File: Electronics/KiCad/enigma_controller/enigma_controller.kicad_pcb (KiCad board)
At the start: 6 copper layers, 267.3 x 149.5 mm, 46 parts, among them IC1 SN74LVC257ADR, IC10 MCP23017-E_SO, IC2 SN74LVC257ADR, IC3 SN74LVC257ADR, IC4 SN74LVC257ADR, IC5 SN74LVC257ADR, IC6 SN74LVC257ADR, IC7 SN74LVC257ADR, IC9 MCP23017-E_SO, J1 Conn_02x07_Odd_Even, J10 0936263006, J11 Conn_02x05_Odd_Even, J12 Conn_01x02, J13 Conn_01x02, J14 USB_C_Receptacle_PowerOnly_6P, J15 Conn_01x02, J16 Conn_01x02, J17 Conn_01x02, J18 Conn_01x02, J19 Conn_01x02, J2 Conn_02x07_Odd_Even, J20 Conn_01x02, J21 Conn_02x05_Odd_Even, J22 Conn_02x05_Odd_Even, J23 Conn_01x02, J24 Conn_01x02, J3 USB1040-GF-L-B, J4 Conn_01x02, J5 46765-0301, J6 Conn_02x05_Odd_Even, J7 Conn_02x07_Odd_Even, J8 USB3_A_Stacked, J9 Conn_02x07_Odd_Even, M1 Fan_4pin

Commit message: Re-organised PCB Layout for better usage of space.
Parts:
- moved BT1 170.6 mm to (220.8, 58.1), turned to -90 degrees
- moved J4 127.9 mm to (267.5, 19.6)
- moved LED2 127.9 mm to (255.1, 19.3)
- moved R2 127.9 mm to (255.1, 22.3)
- moved J12 127.9 mm to (271.9, 19.6)
- moved J13 127.9 mm to (276.1, 19.6)
- moved LED1 127.9 mm to (251.0, 19.3)
- moved R1 127.9 mm to (251.0, 22.4)
- moved LED87 127.9 mm to (259.4, 19.3)
- moved R89 127.9 mm to (259.4, 22.3)
- moved S2 105.0 mm to (219.3, 22.2)
- moved S1 105.0 mm to (209.5, 22.1)
- moved R3 95.9 mm to (232.7, 157.0)
- moved H1 95.1 mm to (214.0, 88.7)
- moved J8 94.4 mm to (212.1, 152.6)
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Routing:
- net Net-(J10-A_YELLOW): track 8.55 -> 5.77 mm
- net Net-(J10-A_GREEN): track 5.99 -> 3.28 mm
- added copper zone on In3.Cu, net +3V3
- added copper zone on In2.Cu, net +5V
- added copper zone on In4.Cu, net /SHIELD
- added copper zone on In1.Cu, net GND
- removed copper zone on In4.Cu, net +3V3
- removed copper zone on In1.Cu, net +5V
- removed copper zone on In2.Cu, net /SHIELD
- removed copper zone on In3.Cu, net GND
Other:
- board text added: "Board Stackup L1 = Fast Signals + JTAG L2 = GND L3 = +5V L4 = +3V3 L5 = SHIELD L6 = Slow Signals"

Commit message: Controller updates based on CM5IO board schematics.
Added some extra datasheets.
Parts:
- removed J12, J13, J4: Conn_01x02, Connector_PinHeader_2.54mm:PinHeader_1x02_P2.54mm_Vertical
- removed R89: ERA2AEB201X, Enigma_Components:ERA2AED122X
- added C1: 100nF, PCM_JLCPCB:C_0402, F.Cu at (255.0, 118.4)
- added C10: 100nF, PCM_JLCPCB:C_0402, F.Cu at (72.2, 141.5)
- added C11: 100nF, PCM_JLCPCB:C_0402, F.Cu at (40.8, 99.5)
- added C12: 100nF, PCM_JLCPCB:C_0402, F.Cu at (69.5, 84.7)
- added C13: 100nF, PCM_JLCPCB:C_0402, F.Cu at (135.7, 72.7)
- added C14: 100nF, PCM_JLCPCB:C_0402, F.Cu at (41.4, 70.5)
- added C15: 100nF, PCM_JLCPCB:C_0402, F.Cu at (42.1, 48.5)
- added C16: 100nF, PCM_JLCPCB:C_0402, F.Cu at (75.4, 31.6)
- added C17: 100nF, PCM_JLCPCB:C_0402, F.Cu at (135.8, 91.3)
- added C18: 10uF, PCM_JLCPCB:C_0603, F.Cu at (165.9, 119.9)
- added C19: 10uF, PCM_JLCPCB:C_0603, F.Cu at (166.0, 134.5)
- added C2: 100nF, PCM_JLCPCB:C_0402, F.Cu at (255.0, 119.6)
- added C3: 10uF, PCM_JLCPCB:C_0603, F.Cu at (166.0, 136.5)
- added C4: 100uF_25V, Capacitor_THT:CP_Radial_D6.3mm_P2.50mm, F.Cu at (166.8, 130.0)
- added C7: 100nF, PCM_JLCPCB:C_0402, F.Cu at (192.2, 139.5)
- added C8: 100nF, PCM_JLCPCB:C_0402, F.Cu at (196.5, 139.5)
- added C9: 100nF, PCM_JLCPCB:C_0402, F.Cu at (40.0, 118.3)
- added H2: MountingHole_Pad, MountingHole:MountingHole_4.3mm_M4_Pad_Via, F.Cu at (43.3, 34.7)
- added H3: MountingHole_Pad, MountingHole:MountingHole_4.3mm_M4_Pad_Via, F.Cu at (43.3, 142.0)
- added H4: MountingHole_Pad, MountingHole:MountingHole_4.3mm_M4_Pad_Via, F.Cu at (257.8, 34.7)
- added H5: MountingHole_Pad, MountingHole:MountingHole_4.3mm_M4_Pad_Via, F.Cu at (134.5, 118.9)
- added H6: MountingHole_Pad, MountingHole:MountingHole_4.3mm_M4_Pad_Via, F.Cu at (257.8, 142.0)
- added H7: MountingHole_Pad, MountingHole:MountingHole_4.3mm_M4_Pad_Via, F.Cu at (169.5, 65.7)
- added IC11: RT9742SNGV, Enigma_Components:SOT95P279X130-3N, F.Cu at (194.3, 140.2)
- added IC8: AP22653W6-7, Enigma_Components:SOT95P280X145-6N, F.Cu at (165.8, 123.3)
- added J25: Conn_01x02, Connector_PinHeader_2.54mm:PinHeader_1x02_P2.54mm_Vertical, F.Cu at (258.4, 45.0)
- added J26: Conn_01x02, Connector_PinHeader_2.54mm:PinHeader_1x02_P2.54mm_Vertical, F.Cu at (258.4, 81.4)
- added J27: Conn_01x02, Connector_PinHeader_2.54mm:PinHeader_1x02_P2.54mm_Vertical, F.Cu at (96.9, 70.3)
- added J28: Conn_02x03_Odd_Even, Connector_PinHeader_2.54mm:PinHeader_2x03_P2.54mm_Vertical, F.Cu at (240.3, 36.9)
- added R10: 1kΩ, PCM_JLCPCB:R_0402, F.Cu at (258.5, 91.3)
- added R5: 2.2kΩ, PCM_JLCPCB:R_0402, F.Cu at (255.3, 112.3)
- added R6: 2.2kΩ, PCM_JLCPCB:R_0402, F.Cu at (218.2, 86.6)
- added R7: 2.2kΩ, PCM_JLCPCB:R_0402, F.Cu at (219.2, 93.4)
- added R8: 10kΩ, PCM_JLCPCB:R_0402, F.Cu at (190.3, 73.8)
- added R9: 15kΩ, PCM_JLCPCB:R_0402, F.Cu at (165.3, 126.0)
- R3, R4: value ERA2AEB201X -> 470Ω; footprint Enigma_Components:ERA2AED122X -> PCM_JLCPCB:R_0402
- moved J17 183.2 mm to (96.9, 120.3), turned to 0 degrees
- moved IC6 109.7 mm to (47.9, 49.8), turned to 90 degrees
- moved IC7 100.1 mm to (74.1, 37.4)
- moved IC5 96.8 mm to (47.2, 71.7), turned to 90 degrees
- moved J3 92.7 mm to (184.3, 113.1), turned to -90 degrees
- moved IC2 86.2 mm to (73.3, 135.6), turned to 180 degrees
- moved LED2 80.4 mm to (261.5, 99.4), turned to 180 degrees
- moved IC3 78.5 mm to (46.8, 100.7), turned to 90 degrees
- moved R2 77.2 mm to (258.5, 99.4), turned to 180 degrees
- moved LED1 76.7 mm to (261.5, 95.3), turned to 180 degrees
- moved R1 73.3 mm to (258.4, 95.3), turned to 180 degrees
- moved LED87 72.0 mm to (261.5, 91.3), turned to 180 degrees
- moved IC1 68.1 mm to (46.1, 119.5), turned to 90 degrees
- moved IC4 65.1 mm to (75.3, 86.0), turned to 90 degrees
- moved M1 60.1 mm to (183.2, 77.6)
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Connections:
- H1 pad 111: +3V3 -> /VBUS_EN
- H1 pad 20: Net-(H1A-EEPROM_nWP) -> /EEPROM_nWP
- H1 pad 35: unconnected-(H1A-ID_SC-Pad35) -> Net-(H1A-ID_SC)
- H1 pad 36: unconnected-(H1A-ID_SD-Pad36) -> Net-(H1A-ID_SD)
- H1 pad 89: Net-(H1A-WL_nDisable) -> /WL_nDisable
- H1 pad 91: Net-(H1A-BT_nDisable) -> /BT_nDisable
- J3 pad 1: +5V -> /VBUS
- J5 pad 19: +5V -> /HDMI_5V
- J8 pad 1: +5V -> /VBUS
- J8 pad 10: +5V -> /VBUS
- S1 pad 1: unconnected-(S1-COM-Pad1) -> GND
- S2 pad 1: unconnected-(S2-COM-Pad1) -> GND
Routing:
- net Net-(J10-A_YELLOW): track 5.77 -> 0.00 mm
- net Net-(J10-A_GREEN): track 3.28 -> 0.00 mm
- net +3V3: track 2.71 -> 0.00 mm, vias 2 -> 0
- net Net-(LED1-Pad2): track 1.78 -> 0.00 mm
- net Net-(LED87-Pad2): track 1.74 -> 0.00 mm
- net Net-(LED2-Pad2): track 1.74 -> 0.00 mm
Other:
- board size 267.3 x 149.5 mm -> 227.9 x 120.8 mm

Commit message: PCB Layout [AS-Review-1]
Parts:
- moved H1 41.8 mm to (190.3, 93.7), turned to -90 degrees
- moved C17 34.7 mm to (169.9, 84.6)
- moved IC10 34.7 mm to (162.8, 67.9)
- moved IC9 34.7 mm to (162.8, 86.5)
- moved C13 34.7 mm to (169.8, 66.0)
- moved J3 29.7 mm to (165.3, 135.9), turned to 90 degrees
- moved M1 25.4 mm to (203.7, 62.8), turned to 180 degrees
- moved BT1 24.9 mm to (230.3, 55.2), turned to 0 degrees
- moved H7 24.6 mm to (189.1, 50.8)
- moved C3 23.4 mm to (160.6, 113.7), turned to 90 degrees
- moved C19 21.1 mm to (162.5, 113.7), turned to 90 degrees
- moved H4 15.6 mm to (242.6, 30.9)
- moved LED2 15.6 mm to (246.3, 95.7)
- moved S1 15.6 mm to (205.9, 30.4)
- moved H6 15.6 mm to (242.6, 138.3)
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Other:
- board size 227.9 x 120.8 mm -> 199.9 x 120.8 mm

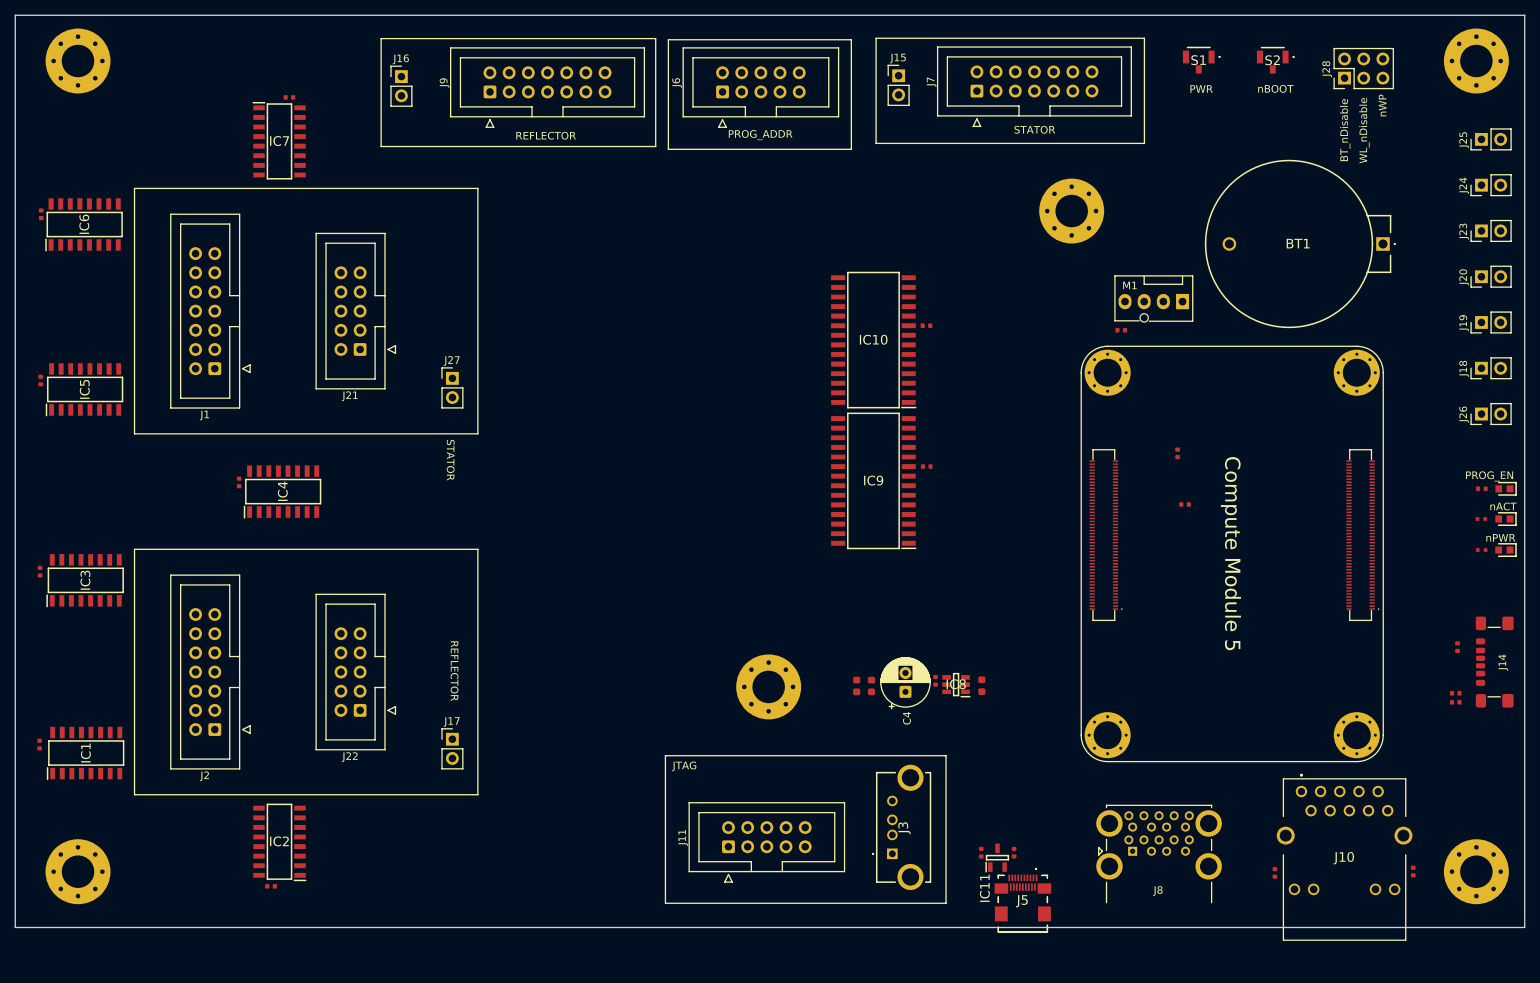
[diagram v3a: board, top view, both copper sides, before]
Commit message: Added ESD Protection.
Also updated some components to follow reference CM5IO board.
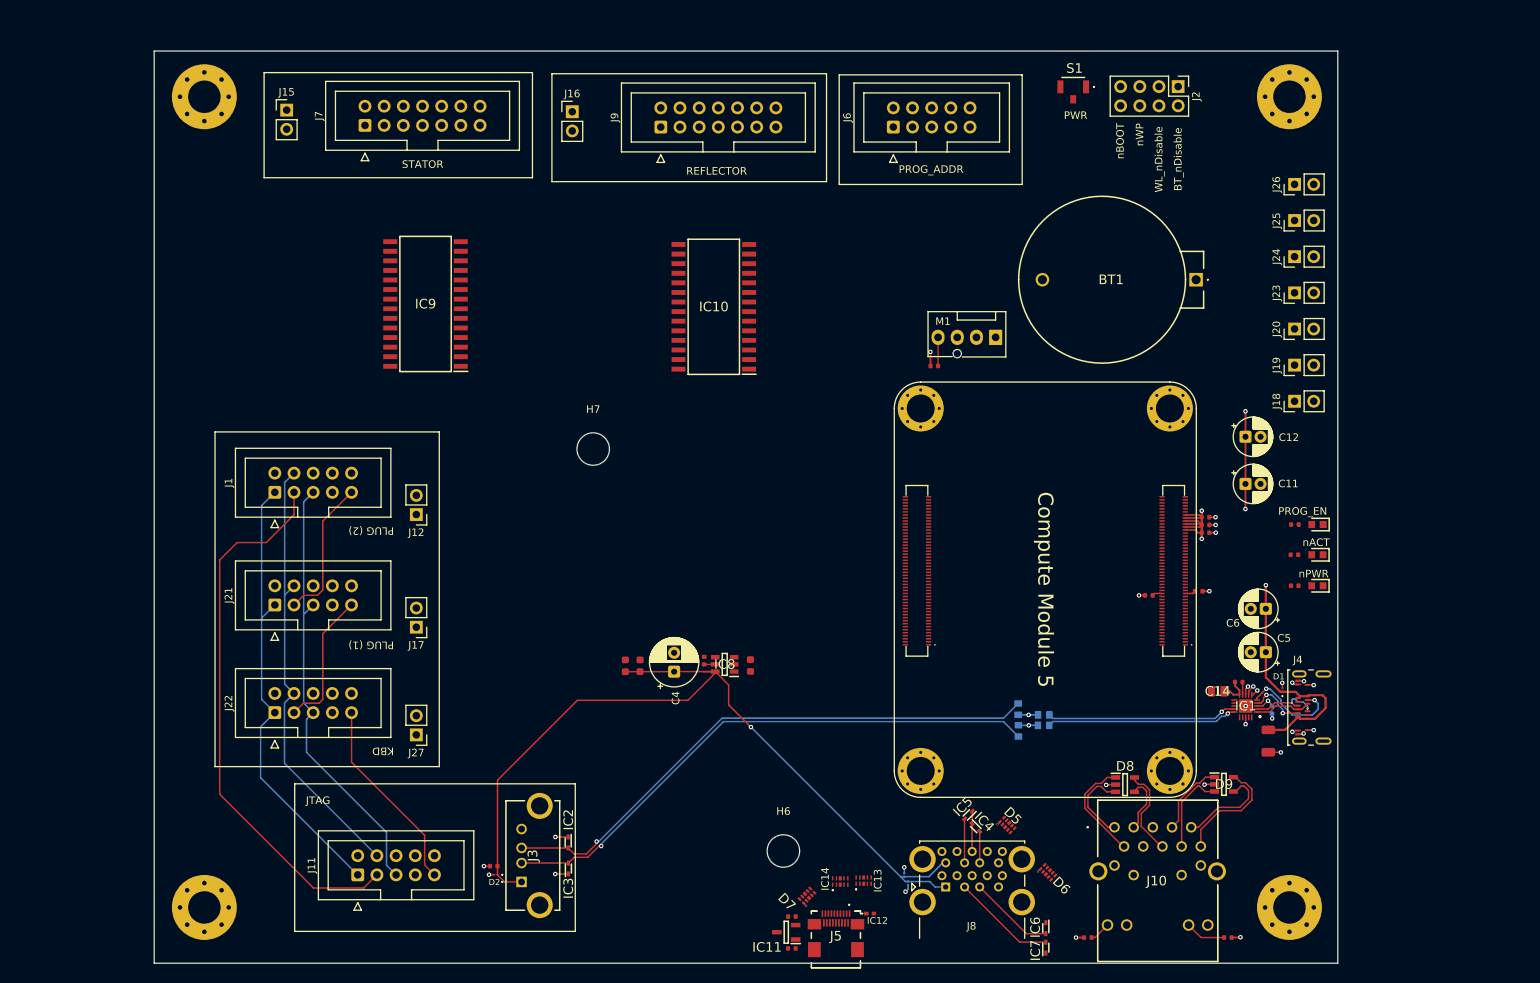
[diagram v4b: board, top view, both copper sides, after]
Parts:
- removed C10, C17: 100nF, PCM_JLCPCB:C_0402
- removed J14: USB_C_Receptacle_PowerOnly_6P, Connector_USB:USB_C_Receptacle_GCT_USB4135-GF-A_6P_TopMnt_Horizontal
- removed J28: Conn_02x03_Odd_Even, Connector_PinHeader_2.54mm:PinHeader_2x03_P2.54mm_Vertical
- removed S2: B3U-1100PM, Enigma_Components:B3U1100PM
- added C5: 4.7uF 50V, Capacitor_THT:CP_Radial_D5.0mm_P2.00mm, F.Cu at (214.8, 109.2)
- added C6: 4.7uF 50V, Capacitor_THT:CP_Radial_D5.0mm_P2.00mm, F.Cu at (214.8, 103.5)
- added D1: ESD441DPLR, Enigma_Components:ESD441DPLR, F.Cu at (217.0, 114.2)
- added D2: ESD441DPLR, Enigma_Components:ESD441DPLR, F.Cu at (112.8, 138.7)
- added D3: ESD441DPLR, Enigma_Components:ESD441DPLR, B.Cu at (166.9, 138.7)
- added D4: ESD441DPLR, Enigma_Components:ESD441DPLR, B.Cu at (167.4, 139.8)
- added D5: TPD4E02B04DQAR, Enigma_Components:DQA(R-PUSON-N10), F.Cu at (180.5, 132.1)
- added D6: TPD4E02B04DQAR, Enigma_Components:DQA(R-PUSON-N10), F.Cu at (185.9, 138.4)
- added D7: TPD4E05U06DQAR, Enigma_Components:DQA(R-PUSON-N10), F.Cu at (154.0, 141.5)
- added D8: ESDS314DBVR, Enigma_Components:SOT95P280X145-5N, F.Cu at (196.1, 126.8)
- added D9: ESDS314DBVR, Enigma_Components:SOT95P280X145-5N, F.Cu at (209.2, 126.7)
- added IC12: TPD1E05U06DPYT, Enigma_Components:TPD1E05U06DPYT, F.Cu at (162.4, 143.8)
- added IC13: ESD224DQAR, Enigma_Components:ESD224DQAR, F.Cu at (161.5, 139.5)
- added IC14: ESD224DQAR, Enigma_Components:ESD224DQAR, F.Cu at (158.4, 139.6)
- added J12: Conn_01x02, Connector_PinHeader_2.54mm:PinHeader_1x02_P2.54mm_Vertical, F.Cu at (102.3, 91.0)
- added J4: USB_C_Receptacle_USB2.0_16P, Connector_USB:USB_C_Receptacle_Amphenol_124019772112A, F.Cu at (222.2, 116.6)
- added R11: RCA06030000ZSEA, Enigma_Components:RESC1608X50N, B.Cu at (182.0, 116.8)
- added R12: RCA06030000ZSEA, Enigma_Components:RESC1608X50N, B.Cu at (185.3, 117.5)
- added R13: RCA06030000ZSEA, Enigma_Components:RESC1608X50N, B.Cu at (182.0, 119.6)
- added R14: RCA06030000ZSEA, Enigma_Components:RESC1608X50N, B.Cu at (185.3, 118.9)
- C11, C12: value 100nF -> 4.7uF 50V; footprint PCM_JLCPCB:C_0402 -> Capacitor_THT:CP_Radial_D5.0mm_P2.00mm
- C13: value 100nF -> 2.2uF; footprint PCM_JLCPCB:C_0402 -> PCM_JLCPCB:C_1206
- C14: value 100nF -> CL21B105KAFNNNG; footprint PCM_JLCPCB:C_0402 -> Enigma_Components:CAPC2012X135N
- C15: moved to B.Cu
- H6, H7: value MountingHole_Pad -> MountingHole; footprint MountingHole:MountingHole_4.3mm_M4_Pad_Via -> MountingHole:MountingHole_4.3mm_M4
- IC1: value SN74LVC257ADR -> TPD8S300ARUKR; footprint Enigma_Components:SOIC127P600X175-16N -> Enigma_Components:QFN40P300X300X80-21N-D
- IC2, IC3, IC4, IC5, IC6, IC7: value SN74LVC257ADR -> ESD321DYAR; footprint Enigma_Components:SOIC127P600X175-16N -> Enigma_Components:SODFL1608X77N
- J1: value Conn_02x07_Odd_Even -> Conn_02x05_Odd_Even; footprint Connector_IDC:IDC-Header_2x07_P2.54mm_Vertical -> Connector_IDC:IDC-Header_2x05_P2.54mm_Vertical
- J10: value 0936263006 -> A70-112-331N126; footprint Enigma_Components:0936263006 -> Enigma_Components:A70112331N126
- J2: value Conn_02x07_Odd_Even -> Conn_02x04_Odd_Even; footprint Connector_IDC:IDC-Header_2x07_P2.54mm_Vertical -> Connector_PinHeader_2.54mm:PinHeader_2x04_P2.54mm_Vertical
- R1, R2: value ERA2AEB201X -> 470Ω; footprint Enigma_Components:ERA2AED122X -> PCM_JLCPCB:R_0402
- R5: value 2.2kΩ -> 100kΩ
- moved C15 175.7 mm to (215.6, 116.9), turned to 90 degrees
- moved C14 161.2 mm to (208.4, 114.4), turned to 0 degrees
- moved C11 160.1 mm to (212.1, 86.9), turned to 0 degrees
- moved IC6 157.7 mm to (185.6, 145.8), turned to -90 degrees
- moved C9 157.3 mm to (206.8, 91.4), turned to 0 degrees
- moved IC1 153.7 mm to (212.1, 116.4), turned to 180 degrees
- moved J2 153.4 mm to (203.2, 34.3), turned to -90 degrees
- moved IC7 147.3 mm to (185.6, 148.4), turned to 90 degrees
- moved C12 133.4 mm to (212.1, 80.7), turned to 0 degrees
- moved IC5 129.8 mm to (175.4, 130.8), turned to -135 degrees
- moved C16 105.3 mm to (112.5, 137.6), turned to 0 degrees
- moved IC4 101.9 mm to (176.4, 132.4), turned to -45 degrees
- moved H6 91.8 mm to (150.9, 135.6)
- moved J15 81.2 mm to (85.1, 37.4)
- moved J7 81.2 mm to (95.5, 39.5)
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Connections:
- net /HDMI0_CEC renamed /enigma_controller_HS/HDMI0_CEC
- net /HDMI0_HOT_PLUG renamed /enigma_controller_HS/HDMI0_HOT_PLUG
- net /HDMI0_SCL renamed /enigma_controller_HS/HDMI0_SCL
- net /HDMI0_SDA renamed /enigma_controller_HS/HDMI0_SDA
- net /HDMI_5V renamed /enigma_controller_HS/HDMI_5V
- net /USB3_0_RX_N renamed /enigma_controller_HS/USB3_0_RX_N
- net /USB3_0_RX_P renamed /enigma_controller_HS/USB3_0_RX_P
- net /USB3_0_TX_N renamed /enigma_controller_HS/USB3_0_TX_N
- net /USB3_0_TX_P renamed /enigma_controller_HS/USB3_0_TX_P
- net /USB3_1_RX_N renamed /enigma_controller_HS/USB3_1_RX_N
- net /USB3_1_RX_P renamed /enigma_controller_HS/USB3_1_RX_P
- net /USB3_1_TX_N renamed /enigma_controller_HS/USB3_1_TX_N
- net /USB3_1_TX_P renamed /enigma_controller_HS/USB3_1_TX_P
- net /VBUS_EN renamed /enigma_controller_HS/VBUS_EN
- C13 pad 1: +3V3 -> +5V
- C14 pad 1: +3V3 -> GND
- C14 pad 2: GND -> +3V3
- C15 pad 2: GND -> Net-(IC1-VBIAS)
- C16 pad 1: +3V3 -> GND
- C16 pad 2: GND -> /VBUS
- C9 pad 1: +3V3 -> +5V
- H1 pad 103: /JTAG_USB_N -> /USB_DN
- H1 pad 105: /JTAG_USB_P -> /USB_DP
- H1 pad 134: /USB3_0_DP -> /enigma_controller_HS/USB3_0_DP
- H1 pad 136: /USB3_0_DM -> /enigma_controller_HS/USB3_0_DM
- H1 pad 163: /USB3_1_DP -> /enigma_controller_HS/USB3_1_DP
- H1 pad 165: /USB3_1_DM -> /enigma_controller_HS/USB3_1_DM
- H1 pad 170: /HDMI0_TX2_P -> /enigma_controller_HS/HDMI0_TX2_P
- H1 pad 172: /HDMI0_TX2_N -> /enigma_controller_HS/HDMI0_TX2_N
- H1 pad 176: /HDMI0_TX1_P -> /enigma_controller_HS/HDMI0_TX1_P
- H1 pad 178: /HDMI0_TX1_N -> /enigma_controller_HS/HDMI0_TX1_N
- H1 pad 182: /HDMI0_TX0_P -> /enigma_controller_HS/HDMI0_TX0_P
- H1 pad 184: /HDMI0_TX0_N -> /enigma_controller_HS/HDMI0_TX0_N
- H1 pad 188: /HDMI0_CLK_P -> /enigma_controller_HS/HDMI0_CLK_P
- H1 pad 190: /HDMI0_CLK_N -> /enigma_controller_HS/HDMI0_CLK_N
- H1 pad 93: Net-(H1A-nRPIBOOT) -> /nRPIBOOT
- IC1 pad 1: /PROG_EN -> /C_D+
- IC1 pad 10: /enigma_controller_prog/pBIN_IN_A3 -> +3V3
- IC1 pad 11: /enigma_controller_prog/rBIN_IN_A3 -> /PD_CC2
- IC1 pad 12: /oBIN_IN_A4 -> /PD_CC1
- IC1 pad 13: /enigma_controller_prog/pBIN_IN_A4 -> GND
- IC1 pad 14: /enigma_controller_prog/rBIN_IN_A4 -> /FLASH_D+
- IC1 pad 15: GND -> /FLASH_D-
- IC1 pad 16: +3V3 -> unconnected-(IC1-D4-Pad16)
- IC1 pad 2: /enigma_controller_prog/rBIN_IN_A1 -> /C_D-
- IC1 pad 3: /enigma_controller_prog/pBIN_IN_A1 -> Net-(IC1-VBIAS)
- IC1 pad 4: /oBIN_IN_A1 -> /C_CC1
- IC1 pad 5: /enigma_controller_prog/rBIN_IN_A2 -> /C_CC2
- IC1 pad 6: /enigma_controller_prog/pBIN_IN_A2 -> GND
- IC1 pad 7: /oBIN_IN_A2 -> GND
- IC1 pad 9: /oBIN_IN_A3 -> Net-(IC1-~{FLT})
- IC10 pad 1: /enigma_controller_prog/pBIN_IN_B1 -> /pBIN_IN_B1
- IC10 pad 2: /enigma_controller_prog/pBIN_IN_B2 -> /pBIN_IN_B2
- IC10 pad 21: /enigma_controller_prog/pBIN_OUT_B1 -> /pBIN_OUT_B1
- IC10 pad 22: /enigma_controller_prog/pBIN_OUT_B2 -> /pBIN_OUT_B2
- IC10 pad 23: /enigma_controller_prog/pBIN_OUT_B3 -> /pBIN_OUT_B3
- IC10 pad 24: /enigma_controller_prog/pBIN_OUT_B4 -> /pBIN_OUT_B4
- IC10 pad 25: /enigma_controller_prog/pBIN_OUT_B5 -> /pBIN_OUT_B5
- IC10 pad 26: /enigma_controller_prog/pBIN_OUT_B6 -> /pBIN_OUT_B6
- IC10 pad 27: /enigma_controller_prog/pBIN_OUT_nOE_B -> /pBIN_OUT_nOE_B
- IC10 pad 3: /enigma_controller_prog/pBIN_IN_B3 -> /pBIN_IN_B3
- IC10 pad 4: /enigma_controller_prog/pBIN_IN_B4 -> /pBIN_IN_B4
- IC10 pad 5: /enigma_controller_prog/pBIN_IN_B5 -> /pBIN_IN_B5
- IC10 pad 6: /enigma_controller_prog/pBIN_IN_B6 -> /pBIN_IN_B6
- IC10 pad 7: /enigma_controller_prog/pBIN_IN_nOE_B -> /pBIN_IN_nOE_B
- IC2 pad 1: /PROG_EN -> GND
- IC2 pad 2: /enigma_controller_prog/rBIN_IN_A5 -> /JTAG_USB_P
- IC3 pad 1: /PROG_EN -> GND
- IC3 pad 2: /enigma_controller_prog/rBIN_OUT_A3 -> /JTAG_USB_N
- IC4 pad 1: /PROG_EN -> GND
- IC4 pad 2: /enigma_controller_prog/rBIN_OUT_B1 -> /enigma_controller_HS/USB3_1_DP
- IC5 pad 1: /PROG_EN -> GND
- IC5 pad 2: /enigma_controller_prog/rBIN_OUT_B5 -> /enigma_controller_HS/USB3_1_DM
- IC6 pad 1: /PROG_EN -> GND
- IC6 pad 2: /enigma_controller_prog/rBIN_IN_B3 -> /enigma_controller_HS/USB3_0_DP
- IC7 pad 1: /PROG_EN -> GND
- IC7 pad 2: /enigma_controller_prog/rBIN_IN_nOE_A -> /enigma_controller_HS/USB3_0_DM
- IC9 pad 1: /enigma_controller_prog/pBIN_IN_A1 -> /pBIN_IN_A1
- IC9 pad 19: /EXP1_INT_A -> /EXP1_INT_B
- IC9 pad 2: /enigma_controller_prog/pBIN_IN_A2 -> /pBIN_IN_A2
- IC9 pad 20: /EXP1_INT_B -> /EXP1_INT_A
- IC9 pad 21: /enigma_controller_prog/pBIN_OUT_A1 -> /pBIN_OUT_A1
- IC9 pad 22: /enigma_controller_prog/pBIN_OUT_A2 -> /pBIN_OUT_A2
- IC9 pad 23: /enigma_controller_prog/pBIN_OUT_A3 -> /pBIN_OUT_A3
- IC9 pad 24: /enigma_controller_prog/pBIN_OUT_A4 -> /pBIN_OUT_A4
- IC9 pad 25: /enigma_controller_prog/pBIN_OUT_A5 -> /pBIN_OUT_A5
- IC9 pad 26: /enigma_controller_prog/pBIN_OUT_A6 -> /pBIN_OUT_A6
- IC9 pad 27: /enigma_controller_prog/pBIN_OUT_nOE_A -> /pBIN_OUT_nOE_A
- IC9 pad 3: /enigma_controller_prog/pBIN_IN_A3 -> /pBIN_IN_A3
- IC9 pad 4: /enigma_controller_prog/pBIN_IN_A4 -> /pBIN_IN_A4
- IC9 pad 5: /enigma_controller_prog/pBIN_IN_A5 -> /pBIN_IN_A5
- IC9 pad 6: /enigma_controller_prog/pBIN_IN_A6 -> /pBIN_IN_A6
- IC9 pad 7: /enigma_controller_prog/pBIN_IN_nOE_A -> /pBIN_IN_nOE_A
- J1 pad 1: /enigma_controller_prog/rBIN_IN_A1 -> /TCK
- J1 pad 10: /enigma_controller_prog/rBIN_OUT_B5 -> GND
- J1 pad 2: /enigma_controller_prog/rBIN_OUT_B1 -> GND
- J1 pad 3: /enigma_controller_prog/rBIN_IN_A2 -> /TDO
- J1 pad 4: /enigma_controller_prog/rBIN_OUT_B2 -> /VCC_JTAG
- J1 pad 5: /enigma_controller_prog/rBIN_IN_A3 -> /TMS
- J1 pad 6: /enigma_controller_prog/rBIN_OUT_B3 -> unconnected-(J1-Pin_6-Pad6)
- J1 pad 7: /enigma_controller_prog/rBIN_IN_A4 -> unconnected-(J1-Pin_7-Pad7)
- J1 pad 8: /enigma_controller_prog/rBIN_OUT_B4 -> unconnected-(J1-Pin_8-Pad8)
- J1 pad 9: /enigma_controller_prog/rBIN_IN_A5 -> /TDX2
- J10 pad MH1: unconnected-(J10-PadMH1) -> /SHIELD
- J10 pad MH2: unconnected-(J10-PadMH2) -> /SHIELD
- J2 pad 1: /enigma_controller_prog/rBIN_OUT_A1 -> GND
- J2 pad 2: /enigma_controller_prog/rBIN_IN_B1 -> /BT_nDisable
- J2 pad 3: /enigma_controller_prog/rBIN_OUT_A2 -> GND
- J2 pad 4: /enigma_controller_prog/rBIN_IN_B2 -> /WL_nDisable
- J2 pad 5: /enigma_controller_prog/rBIN_OUT_A3 -> GND
- J2 pad 6: /enigma_controller_prog/rBIN_IN_B3 -> /EEPROM_nWP
- J2 pad 7: /enigma_controller_prog/rBIN_OUT_A4 -> GND
- J2 pad 8: /enigma_controller_prog/rBIN_IN_B4 -> /nRPIBOOT
- J21 pad 3: /TDX -> /TDX2
- J21 pad 9: /TDI -> /TDX1
- J22 pad 3: /TDO -> /TDX1
- J22 pad 9: /TDX -> /TDI
- J3 pad 5: unconnected-(J3-MH1-Pad5) -> /SHIELD
- J3 pad 6: unconnected-(J3-MH2-Pad6) -> /SHIELD
- J5 pad 11: /HDMI0_TX0_N -> /enigma_controller_HS/TMDS_DATA0-
- J5 pad 12: /HDMI0_CLK_P -> /enigma_controller_HS/TMDS_CLK+
- J5 pad 14: /HDMI0_CLK_N -> /enigma_controller_HS/TMDS_CLK-
- J5 pad 2: unconnected-(J5-UTILITY-Pad2) -> /enigma_controller_HS/HDMI0_UTIL
- J5 pad 3: /HDMI0_TX2_P -> /enigma_controller_HS/TMDS_DATA2+
- J5 pad 5: /HDMI0_TX2_N -> /enigma_controller_HS/TMDS_DATA2-
- J5 pad 6: /HDMI0_TX1_P -> /enigma_controller_HS/TMDS_DATA1+
- J5 pad 8: /HDMI0_TX1_N -> /enigma_controller_HS/TMDS_DATA1-
- J5 pad 9: /HDMI0_TX0_P -> /enigma_controller_HS/TMDS_DATA0+
- J5 pad MP1: unconnected-(J5-PadMP1) -> /SHIELD
- J5 pad MP2: unconnected-(J5-PadMP2) -> /SHIELD
- J5 pad MP3: unconnected-(J5-PadMP3) -> /SHIELD
- J5 pad MP4: unconnected-(J5-PadMP4) -> /SHIELD
- J7 pad 1: /oBIN_IN_A1 -> /pBIN_IN_A1
- J7 pad 10: /oBIN_OUT_B5 -> /pBIN_OUT_B5
- J7 pad 11: /oBIN_IN_A6 -> /pBIN_IN_A6
- J7 pad 12: /oBIN_OUT_B6 -> /pBIN_OUT_B6
- J7 pad 13: /oBIN_IN_nOE_A -> /pBIN_IN_nOE_A
- J7 pad 14: /oBIN_OUT_nOE_B -> /pBIN_OUT_nOE_B
- J7 pad 2: /oBIN_OUT_B1 -> /pBIN_OUT_B1
- J7 pad 3: /oBIN_IN_A2 -> /pBIN_IN_A2
- J7 pad 4: /oBIN_OUT_B2 -> /pBIN_OUT_B2
- J7 pad 5: /oBIN_IN_A3 -> /pBIN_IN_A3
- J7 pad 6: /oBIN_OUT_B3 -> /pBIN_OUT_B3
- J7 pad 7: /oBIN_IN_A4 -> /pBIN_IN_A4
- J7 pad 8: /oBIN_OUT_B4 -> /pBIN_OUT_B4
- J7 pad 9: /oBIN_IN_A5 -> /pBIN_IN_A5
- J8 pad 11: /USB3_1_DM -> /enigma_controller_HS/USB3_1_DM
- J8 pad 12: /USB3_1_DP -> /enigma_controller_HS/USB3_1_DP
- J8 pad 2: /USB3_0_DM -> /enigma_controller_HS/USB3_0_DM
- J8 pad 3: /USB3_0_DP -> /enigma_controller_HS/USB3_0_DP
- J9 pad 1: /oBIN_OUT_A1 -> /pBIN_OUT_A1
- J9 pad 10: /oBIN_IN_B5 -> /pBIN_IN_B5
- J9 pad 11: /oBIN_OUT_A6 -> /pBIN_OUT_A6
- J9 pad 12: /oBIN_IN_B6 -> /pBIN_IN_B6
- J9 pad 13: /oBIN_OUT_nOE_A -> /pBIN_OUT_nOE_A
- J9 pad 14: /oBIN_IN_nOE_B -> /pBIN_IN_nOE_B
- J9 pad 2: /oBIN_IN_B1 -> /pBIN_IN_B1
- J9 pad 3: /oBIN_OUT_A2 -> /pBIN_OUT_A2
- J9 pad 4: /oBIN_IN_B2 -> /pBIN_IN_B2
- J9 pad 5: /oBIN_OUT_A3 -> /pBIN_OUT_A3
- J9 pad 6: /oBIN_IN_B3 -> /pBIN_IN_B3
- J9 pad 7: /oBIN_OUT_A4 -> /pBIN_OUT_A4
- J9 pad 8: /oBIN_IN_B4 -> /pBIN_IN_B4
- J9 pad 9: /oBIN_OUT_A5 -> /pBIN_OUT_A5
- R3 pad 1: Net-(J10-A_GREEN) -> Net-(J10-GREEN_ANODE)
- R4 pad 1: Net-(J10-A_YELLOW) -> Net-(J10-YELLOW_ANODE)
- R5 pad 1: +5V -> +3V3
- R5 pad 2: GND -> Net-(IC1-~{FLT})
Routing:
- net /VBUS: track 0.00 -> 115.3 mm, vias 0 -> 1
- net /JTAG_USB_N: track 0.00 -> 74.5 mm, vias 0 -> 1
- net /JTAG_USB_P: track 0.00 -> 74.5 mm, vias 0 -> 1
- net /TDO: track 0.00 -> 73.0 mm
- net /TCK: track 0.00 -> 60.7 mm
- net /VCC_JTAG: track 0.00 -> 59.0 mm
- net /TMS: track 0.00 -> 58.8 mm
- net +5V: track 0.00 -> 49.5 mm, vias 0 -> 3
- net GND: track 0.00 -> 29.0 mm, vias 0 -> 24
- net /TDI: track 0.00 -> 26.0 mm
- net /FLASH_D-: track 0.00 -> 25.2 mm, vias 0 -> 1
- net /FLASH_D+: track 0.00 -> 25.2 mm, vias 0 -> 1
- net +3V3: track 0.00 -> 23.6 mm, vias 0 -> 8
- net /TDX2: track 0.00 -> 19.1 mm
- net /TDX1: track 0.00 -> 18.6 mm
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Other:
- board size 199.9 x 120.8 mm -> 156.7 x 120.8 mm
- board text added: "Board Stackup L1 = Fast Signals + JTAG L2 = GND (+ SHIELD RING) L3 = +5V L4 = +3V3 L5 = GND (+ SHIELD RING) L6 = Slow Signals + JTAG"
- board text added: "KBD"
- board text added: "PLUG (1)"
- board text added: "PLUG (2)"
- board text removed: "Board Stackup L1 = Fast Signals + JTAG L2 = GND L3 = +5V L4 = +3V3 L5 = SHIELD L6 = Slow Signals"
